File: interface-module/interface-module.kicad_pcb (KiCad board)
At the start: 2 copper layers, 32 parts, among them J4 Conn_01x08, J6 Conn_01x08, Q1 PMOS, Q10 NMOS, Q11 PMOS, Q12 NMOS, Q13 PMOS, Q14 NMOS, Q15 PMOS, Q16 NMOS, Q2 NMOS, Q3 PMOS, Q4 NMOS, Q5 PMOS, Q6 NMOS, Q7 PMOS, Q8 NMOS, Q9 PMOS, U10 TCA9548ARGER, U2 140357145200, U3 140357145200, U4 140357145200, U5 140357145200, U6 140357145200, U7 140357145200, U8 140357145200, U9 140357145200

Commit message: Fixed footprints
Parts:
- added C1: 1u, Capacitor_SMD:C_0603_1608Metric, F.Cu at (148.8, 71.2)
- added C2: 1u, Capacitor_SMD:C_0603_1608Metric, F.Cu at (148.8, 73.8)
- added C3: 10u, Capacitor_SMD:C_0603_1608Metric, F.Cu at (148.8, 76.3)
- added C4: 1u, Capacitor_SMD:C_0603_1608Metric, F.Cu at (148.8, 78.8)
- added C5: 1u, Capacitor_SMD:C_0603_1608Metric, F.Cu at (148.8, 81.3)
- added C6: 10u, Capacitor_SMD:C_0603_1608Metric, F.Cu at (148.8, 83.8)
- added C7: 0.1u, Capacitor_SMD:C_0603_1608Metric, F.Cu at (148.8, 86.3)
- added D1: 1SS396, Package_TO_SOT_SMD:SOT-23-3, F.Cu at (59.5, 133.1)
- added D2: 1SS396, Package_TO_SOT_SMD:SOT-23-3, F.Cu at (59.5, 137.7)
- added D3: 1SS396, Package_TO_SOT_SMD:SOT-23-3, F.Cu at (64.6, 133.1)
- added D4: 1SS396, Package_TO_SOT_SMD:SOT-23-3, F.Cu at (64.6, 137.7)
- added D5: 1SS396, Package_TO_SOT_SMD:SOT-23-3, F.Cu at (69.8, 133.1)
- added D6: 1SS396, Package_TO_SOT_SMD:SOT-23-3, F.Cu at (69.8, 137.7)
- added D7: 1SS396, Package_TO_SOT_SMD:SOT-23-3, F.Cu at (74.9, 133.1)
- added D8: 1SS396, Package_TO_SOT_SMD:SOT-23-3, F.Cu at (74.9, 137.7)
- added R1: 10k, Resistor_SMD:R_0603_1608Metric, F.Cu at (231.0, 70.9)
- added R10: 0, Resistor_SMD:R_0603_1608Metric, F.Cu at (62.9, 143.7)
- added R11: R_ADC_TOP, Resistor_SMD:R_0603_1608Metric, F.Cu at (62.9, 146.2)
- added R12: R_ADC_BTM, Resistor_SMD:R_0603_1608Metric, F.Cu at (62.9, 148.7)
- added R13: R_ADC_NEG, Resistor_SMD:R_0603_1608Metric, F.Cu at (62.9, 151.2)
- added R14: R_ADC_POS, Resistor_SMD:R_0603_1608Metric, F.Cu at (62.9, 153.8)
- added R15: R_ADC_TOP, Resistor_SMD:R_0603_1608Metric, F.Cu at (66.9, 141.2)
- added R16: R_ADC_POS, Resistor_SMD:R_0603_1608Metric, F.Cu at (66.9, 143.7)
- added R17: R_ADC_BTM, Resistor_SMD:R_0603_1608Metric, F.Cu at (66.9, 146.2)
- added R18: R_ADC_NEG, Resistor_SMD:R_0603_1608Metric, F.Cu at (66.9, 148.7)
- added R19: R_ADC_TOP, Resistor_SMD:R_0603_1608Metric, F.Cu at (66.9, 151.2)
- added R2: CFG1, Resistor_SMD:R_0603_1608Metric, F.Cu at (58.9, 141.2)
- added R20: R_ADC_POS, Resistor_SMD:R_0603_1608Metric, F.Cu at (66.9, 153.8)
- added R21: R_ADC_BTM, Resistor_SMD:R_0603_1608Metric, F.Cu at (71.0, 141.2)
- added R22: R_ADC_NEG, Resistor_SMD:R_0603_1608Metric, F.Cu at (71.0, 143.7)
- added R23: R_ADC_TOP, Resistor_SMD:R_0603_1608Metric, F.Cu at (71.0, 146.2)
- added R24: R_ADC_POS, Resistor_SMD:R_0603_1608Metric, F.Cu at (71.0, 148.7)
- added R25: R_ADC_BTM, Resistor_SMD:R_0603_1608Metric, F.Cu at (71.0, 151.2)
- added R26: R_ADC_NEG, Resistor_SMD:R_0603_1608Metric, F.Cu at (71.0, 153.8)
- added R3: 10k, Resistor_SMD:R_0603_1608Metric, F.Cu at (231.0, 73.4)
- added R4: CFG2, Resistor_SMD:R_0603_1608Metric, F.Cu at (58.9, 143.7)
- added R5: 0, Resistor_SMD:R_0603_1608Metric, F.Cu at (58.9, 146.2)
- added R6: 0, Resistor_SMD:R_0603_1608Metric, F.Cu at (58.9, 148.7)
- added R7: 0, Resistor_SMD:R_0603_1608Metric, F.Cu at (58.9, 151.2)
- added R8: 0, Resistor_SMD:R_0603_1608Metric, F.Cu at (58.9, 153.8)
- added R9: 1, Resistor_SMD:R_0603_1608Metric, F.Cu at (62.9, 141.2)
- added SW1: SW_Coded_SH-7050, Button_Switch_THT:Nidec_Copal_SH-7010C, F.Cu at (81.4, 142.8)
- added U11: MCP3464, Package_DFN_QFN:UQFN-20-1EP_3x3mm_P0.4mm_EP1.85x1.85mm, F.Cu at (75.6, 151.8)
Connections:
- U1 pad 20: unconnected-(U1-PB12-Pad20) -> CTRL
- U10 pad 18: unconnected-(U10-A2-Pad18) -> Net-(U10-A2)
- U10 pad 19: unconnected-(U10-SCL-Pad19) -> I2C_SCL
- U10 pad 20: unconnected-(U10-SDA-Pad20) -> I2C_SDA
- U10 pad 21: unconnected-(U10-VCC-Pad21) -> +3V3
- U10 pad 22: unconnected-(U10-A0-Pad22) -> Net-(U10-A0)
- U10 pad 23: unconnected-(U10-A1-Pad23) -> Net-(U10-A1)
- U10 pad 24: unconnected-(U10-~{RESET}-Pad24) -> CTRL
- U10 pad 9: unconnected-(U10-GND-Pad9) -> GND

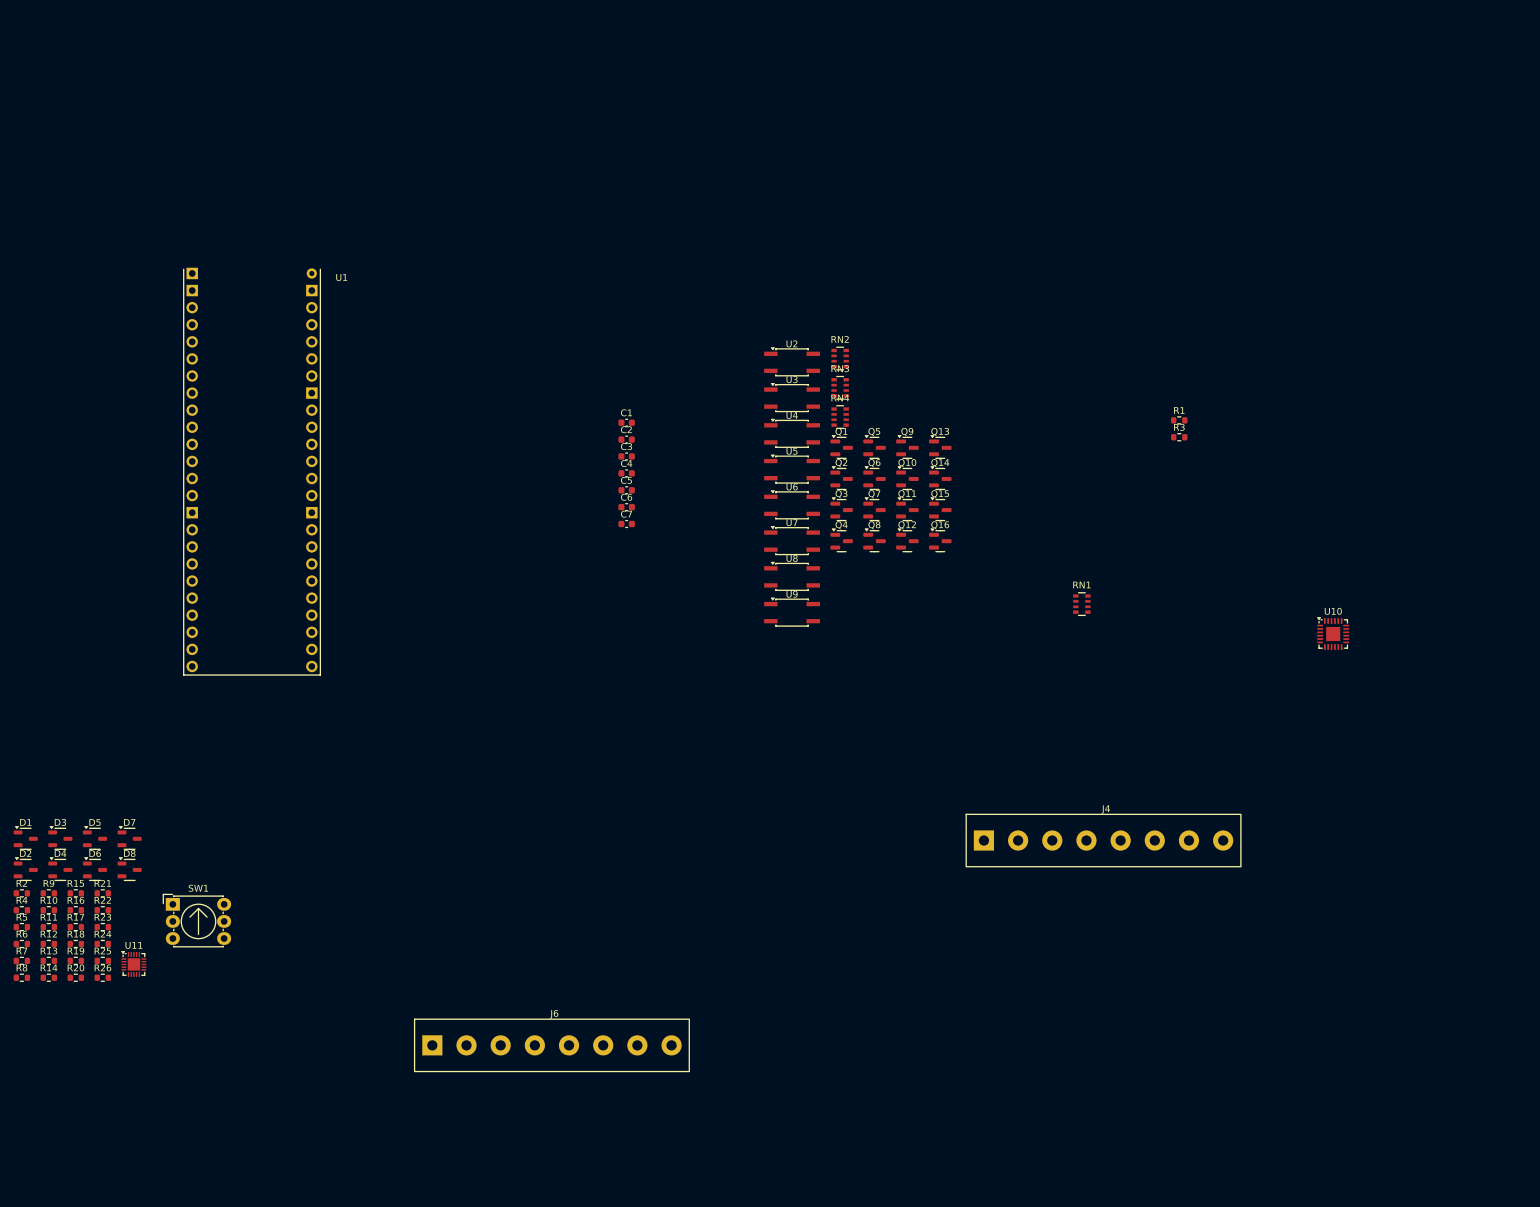
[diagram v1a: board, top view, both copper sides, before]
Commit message: routed most of board
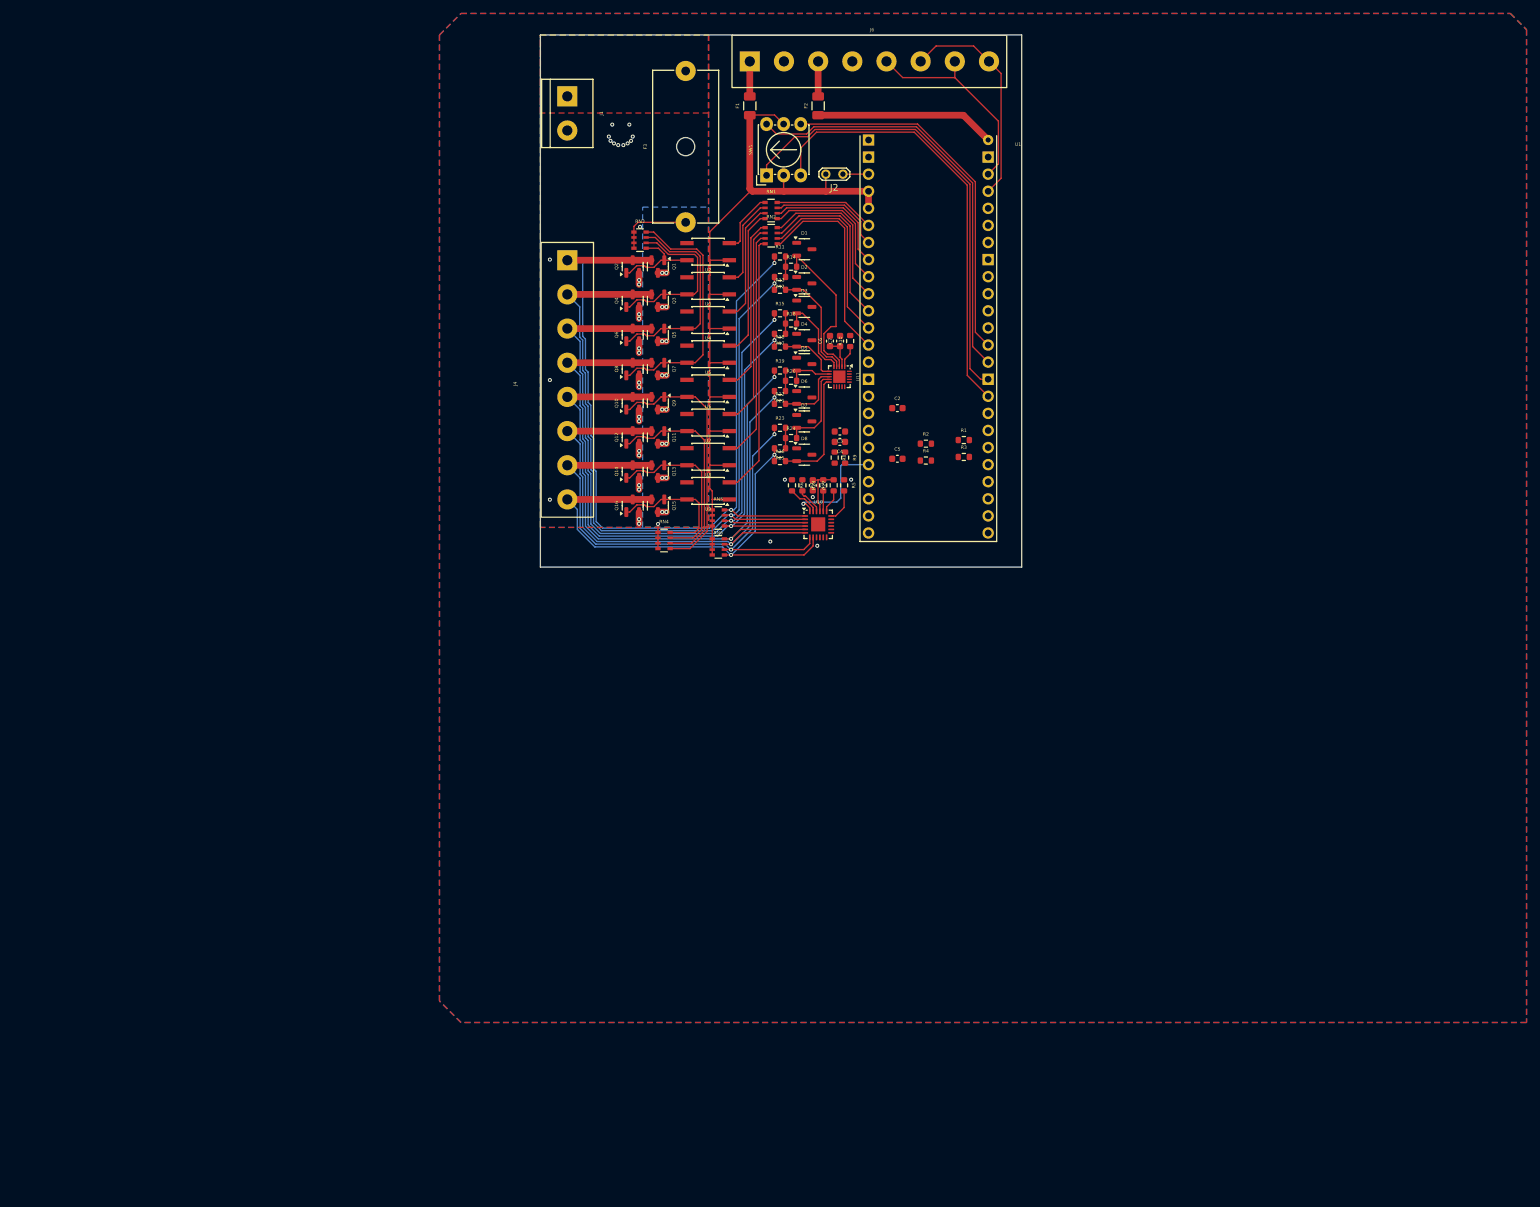
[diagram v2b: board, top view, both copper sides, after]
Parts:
- added F1: 150mA Poly, Fuse:Fuse_1206_3216Metric, F.Cu at (167.1, 24.1)
- added F2: 350mA Poly, Fuse:Fuse_1206_3216Metric, F.Cu at (177.3, 24.1)
- added F3: 15A slow, Fuse:Fuseholder_Cylinder-5x20mm_Schurter_0031_8201_Horizontal_Open, F.Cu at (157.6, 41.5)
- added J1: Conn_01x02, TerminalBlock:TerminalBlock_bornier-2_P5.08mm, F.Cu at (140.0, 22.7)
- added J2: Conn_01x02, TestPoint:TestPoint_2Pads_Pitch2.54mm_Drill0.8mm, F.Cu at (181.0, 34.3)
- added R27: 4k7, Resistor_SMD:R_0603_1608Metric, F.Cu at (179.6, 80.5)
- added R28: 4k7, Resistor_SMD:R_0603_1608Metric, F.Cu at (178.1, 80.5)
- added RN5: 4k7, Resistor_SMD:R_Array_Convex_4x0603, F.Cu at (162.4, 85.4)
- added RN6: 4k7, Resistor_SMD:R_Array_Convex_4x0603, F.Cu at (162.4, 89.7)
- RN1, RN2: value 100 -> 330
- U10: value TCA9548ARGER -> TCA9548
- moved J6 153.7 mm to (167.1, 17.5)
- moved R14 152.8 mm to (173.3, 48.1)
- moved R4 150.1 mm to (193.3, 76.9)
- moved R2 150.1 mm to (193.3, 74.4)
- moved R13 147.5 mm to (171.6, 51.5)
- moved R11 147.5 mm to (171.6, 46.5)
- moved R12 147.1 mm to (171.6, 49.6), turned to 180 degrees
- moved R10 146.1 mm to (182.1, 59.1), turned to 90 degrees
- moved D1 145.2 mm to (175.2, 45.5)
- moved D2 144.9 mm to (175.2, 50.5)
- moved R8 143.5 mm to (179.8, 76.4), turned to -90 degrees
- moved SW1 139.8 mm to (169.6, 34.5), turned to 90 degrees
- moved R5 138.8 mm to (181.2, 80.5), turned to -90 degrees
- moved R20 138.5 mm to (173.3, 65.0)
- moved R16 137.5 mm to (173.3, 56.5)
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- renumbered U9 to U8, U8 to U9
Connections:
- J6 pad 1: VPOW -> Net-(J6-Pin_1)
- J6 pad 2: GNDP -> GND
- J6 pad 3: VBUS -> Net-(J6-Pin_3)
- RN1 pad 2: CTL_OUT_0 -> Net-(RN1B-R2.1)
- RN1 pad 3: Net-(RN1B-R2.1) -> Net-(RN1C-R3.1)
- RN1 pad 4: CTL_OUT_1 -> Net-(RN1D-R4.1)
- RN1 pad 5: Net-(RN1C-R3.1) -> CTL_OUT_3
- RN1 pad 7: Net-(RN1D-R4.1) -> CTL_OUT_1
- RN1 pad 8: CTL_OUT_3 -> CTL_OUT_0
- RN2 pad 2: CTL_OUT_4 -> Net-(RN2B-R2.1)
- RN2 pad 3: Net-(RN2B-R2.1) -> Net-(RN2C-R3.1)
- RN2 pad 4: CTL_OUT_5 -> Net-(RN2D-R4.1)
- RN2 pad 5: Net-(RN2C-R3.1) -> CTL_OUT_7
- RN2 pad 7: Net-(RN2D-R4.1) -> CTL_OUT_5
- RN2 pad 8: CTL_OUT_7 -> CTL_OUT_4
- RN3 pad 2: /outputs/~{ISO_OUT_0} -> VPOW
- RN3 pad 4: /outputs/~{ISO_OUT_1} -> VPOW
- RN3 pad 5: VPOW -> /outputs/~{ISO_OUT_0}
- RN3 pad 6: /outputs/~{ISO_OUT_2} -> /outputs/~{ISO_OUT_1}
- RN3 pad 7: VPOW -> /outputs/~{ISO_OUT_2}
- RN4 pad 2: /outputs/~{ISO_OUT_4} -> VPOW
- RN4 pad 4: /outputs/~{ISO_OUT_5} -> VPOW
- RN4 pad 5: VPOW -> /outputs/~{ISO_OUT_4}
- RN4 pad 6: /outputs/~{ISO_OUT_6} -> /outputs/~{ISO_OUT_5}
- RN4 pad 7: VPOW -> /outputs/~{ISO_OUT_6}
- SW1 pad 1: Net-(U1-PA7) -> Net-(U1-PA5)
- SW1 pad 2: Net-(U1-PA8) -> Net-(U1-PA7)
- SW1 pad 4: Net-(U1-PA9) -> Net-(U1-PA4)
- SW1 pad 8: Net-(U1-PA10) -> Net-(U1-PA6)
- U1 pad 25: Net-(U1-PA8) -> unconnected-(U1-PA8-Pad25)
- U1 pad 26: Net-(U1-PA9) -> unconnected-(U1-PA9-Pad26)
- U1 pad 27: Net-(U1-PA10) -> unconnected-(U1-PA10-Pad27)
- U1 pad 3: unconnected-(U1-BOOTSEL-Pad3) -> Net-(J2-Pin_1)
- U1 pad 33: unconnected-(U1-PA4-Pad33) -> Net-(U1-PA4)
- U1 pad 34: unconnected-(U1-PA5-Pad34) -> Net-(U1-PA5)
- U1 pad 35: unconnected-(U1-PA6-Pad35) -> Net-(U1-PA6)
- U10 pad 1: OUT1/IN0- -> OUT0/IN0+
- U10 pad 2: OUT0/IN0+ -> OUT1/IN0-
- U10 pad 3: OUT3/IN1- -> OUT2/IN1+
- U10 pad 4: OUT2/IN1+ -> OUT3/IN1-
- U10 pad 5: OUT5/IN2- -> OUT4/IN2+
- U10 pad 6: OUT4/IN2+ -> OUT5/IN2-
- U10 pad 7: OUT7/IN3- -> OUT6/IN3+
- U10 pad 8: OUT6/IN3+ -> OUT7/IN3-
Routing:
- net +3V3: track 0.00 -> 132.0 mm
- net OUT0/IN0+: track 0.00 -> 128.7 mm, vias 0 -> 2
- net OUT1/IN0-: track 0.00 -> 121.4 mm, vias 0 -> 2
- net OUT2/IN1+: track 0.00 -> 111.1 mm, vias 0 -> 2
- net OUT3/IN1-: track 0.00 -> 104.8 mm, vias 0 -> 2
- net OUT4/IN2+: track 0.00 -> 95.5 mm, vias 0 -> 2
- net OUT5/IN2-: track 0.00 -> 90.0 mm, vias 0 -> 2
- net OUT6/IN3+: track 0.00 -> 81.2 mm, vias 0 -> 2
- net OUT7/IN3-: track 0.00 -> 76.5 mm, vias 0 -> 2
- net Net-(U1-PA5): track 0.00 -> 68.1 mm
- net Net-(U1-PA4): track 0.00 -> 65.7 mm
- net Net-(U1-PA6): track 0.00 -> 62.7 mm
- net Net-(U1-PA7): track 0.00 -> 54.6 mm
- net Net-(RN2D-R4.1): track 0.00 -> 38.8 mm
- net /outputs/~{ISO_OUT_4}: track 0.00 -> 38.5 mm
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- added copper zone on B.Cu, net GND
- added copper zone on F.Cu, net GND
- added copper zone on B.Cu, net GNDP
- added copper zone on F.Cu, net GNDP
- added copper zone on F.Cu, net Net-(J1-Pin_1)
- added copper zone on B.Cu, net VPOW
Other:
- board outline added: 71.6 x 79.1 mm

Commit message: Finished copper layout
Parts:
- added D10: MMBD717LT1G, Package_TO_SOT_SMD:SOT-323_SC-70, F.Cu at (146.1, 59.8)
- added D11: MMBD717LT1G, Package_TO_SOT_SMD:SOT-323_SC-70, F.Cu at (146.1, 70.0)
- added D12: MMBD717LT1G, Package_TO_SOT_SMD:SOT-323_SC-70, F.Cu at (146.1, 80.1)
- added D9: MMBD717LT1G, Package_TO_SOT_SMD:SOT-323_SC-70, F.Cu at (146.1, 49.5)
- added R29: R_SHUNT, Resistor_SMD:R_0603_1608Metric, F.Cu at (145.1, 49.5)
- added R30: R_SHUNT, Resistor_SMD:R_0603_1608Metric, F.Cu at (145.1, 59.8)
- added R31: R_SHUNT, Resistor_SMD:R_0603_1608Metric, F.Cu at (145.1, 70.0)
- added R32: R_SHUNT, Resistor_SMD:R_0603_1608Metric, F.Cu at (145.1, 80.1)
- added REF**: MountingHole_3.2mm_M3, MountingHole:MountingHole_3.2mm_M3, F.Cu at (195.0, 89.0)
- added REF**: MountingHole_3.2mm_M3, MountingHole:MountingHole_3.2mm_M3, F.Cu at (140.0, 34.0)
- added REF**: MountingHole_3.2mm_M3, MountingHole:MountingHole_3.2mm_M3, F.Cu at (140.0, 89.0)
- added REF**: MountingHole_3.2mm_M3, MountingHole:MountingHole_3.2mm_M3, F.Cu at (195.0, 34.0)
- moved C5 8.83 mm to (180.2, 76.9), turned to 180 degrees
- moved C2 5.54 mm to (186.8, 64.0), turned to -90 degrees
- moved R4 4.44 mm to (197.5, 78.3), turned to -90 degrees
- moved R2 4.20 mm to (197.5, 74.1), turned to 90 degrees
- moved R3 2.01 mm to (199.2, 78.3), turned to 90 degrees
- moved C4 1.87 mm to (180.2, 72.2)
- moved C3 1.87 mm to (180.2, 70.7)
- moved R8 1.87 mm to (179.5, 74.6)
- moved R9 1.87 mm to (181.0, 74.6)
- moved R1 0.33 mm to (199.2, 74.1), turned to -90 degrees
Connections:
- U1 pad 24: +3V3 -> unconnected-(U1-3v3-Pad24)
- U1 pad 44: +3V3 -> unconnected-(U1-3v3-Pad44)
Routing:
- net +3V3: track 132.0 -> 210.7 mm, vias 0 -> 2
- net GNDA: track 0.00 -> 56.1 mm, vias 0 -> 15
- net +3.3VA: track 0.00 -> 55.8 mm, vias 0 -> 11
- net SPI_MOSI: track 0.00 -> 21.0 mm
- net SPI_MISO: track 0.00 -> 18.3 mm
- net SPI_SCK: track 0.00 -> 17.1 mm, vias 0 -> 1
- net I2C_SDA: track 3.04 -> 16.3 mm, vias 0 -> 1
- net CTRL: track 16.6 -> 29.3 mm, vias 1 -> 2
- net I2C_SCL: track 3.47 -> 15.5 mm, vias 0 -> 1
- net /CONFIG1: track 0.00 -> 5.08 mm
- net /CONFIG0: track 0.00 -> 5.08 mm
- net Net-(U1-PA7): track 54.6 -> 58.7 mm
- net Net-(U1-PA6): track 62.7 -> 66.8 mm
- net Net-(U1-PA5): track 68.1 -> 72.2 mm
- net Net-(U1-PA4): track 65.7 -> 69.8 mm
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- added copper zone on B.Cu, net GNDA
- added copper zone on F.Cu, net GNDA
